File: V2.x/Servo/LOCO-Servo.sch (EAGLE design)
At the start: 49 parts, among them IC1 Atmega 328-P, IC2 MCP2515, IC3 LM340MP-05, Q1 8MHz, Q2 16MHz, X2 2X6-A

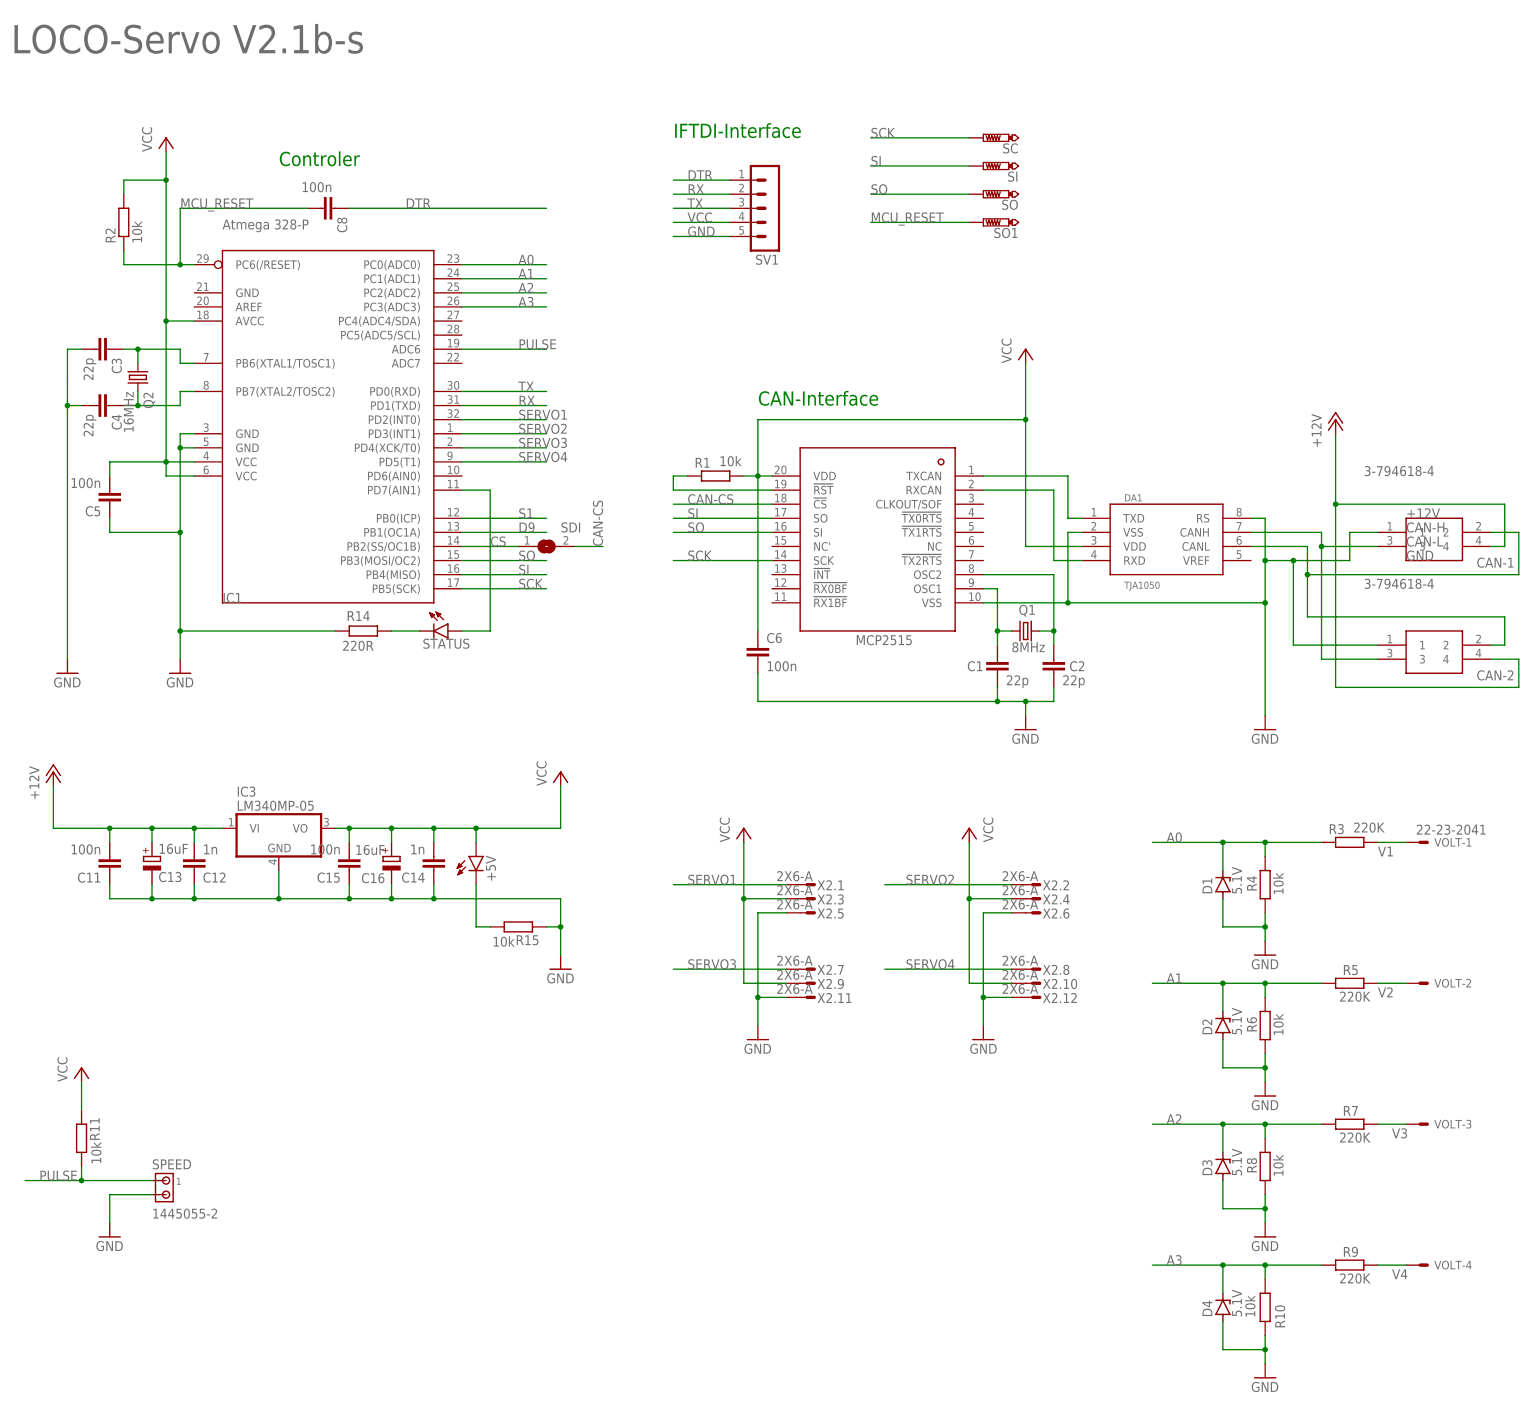
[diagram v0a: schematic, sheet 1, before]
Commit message: added Loco-CAN icon to motor, servo and switch boards
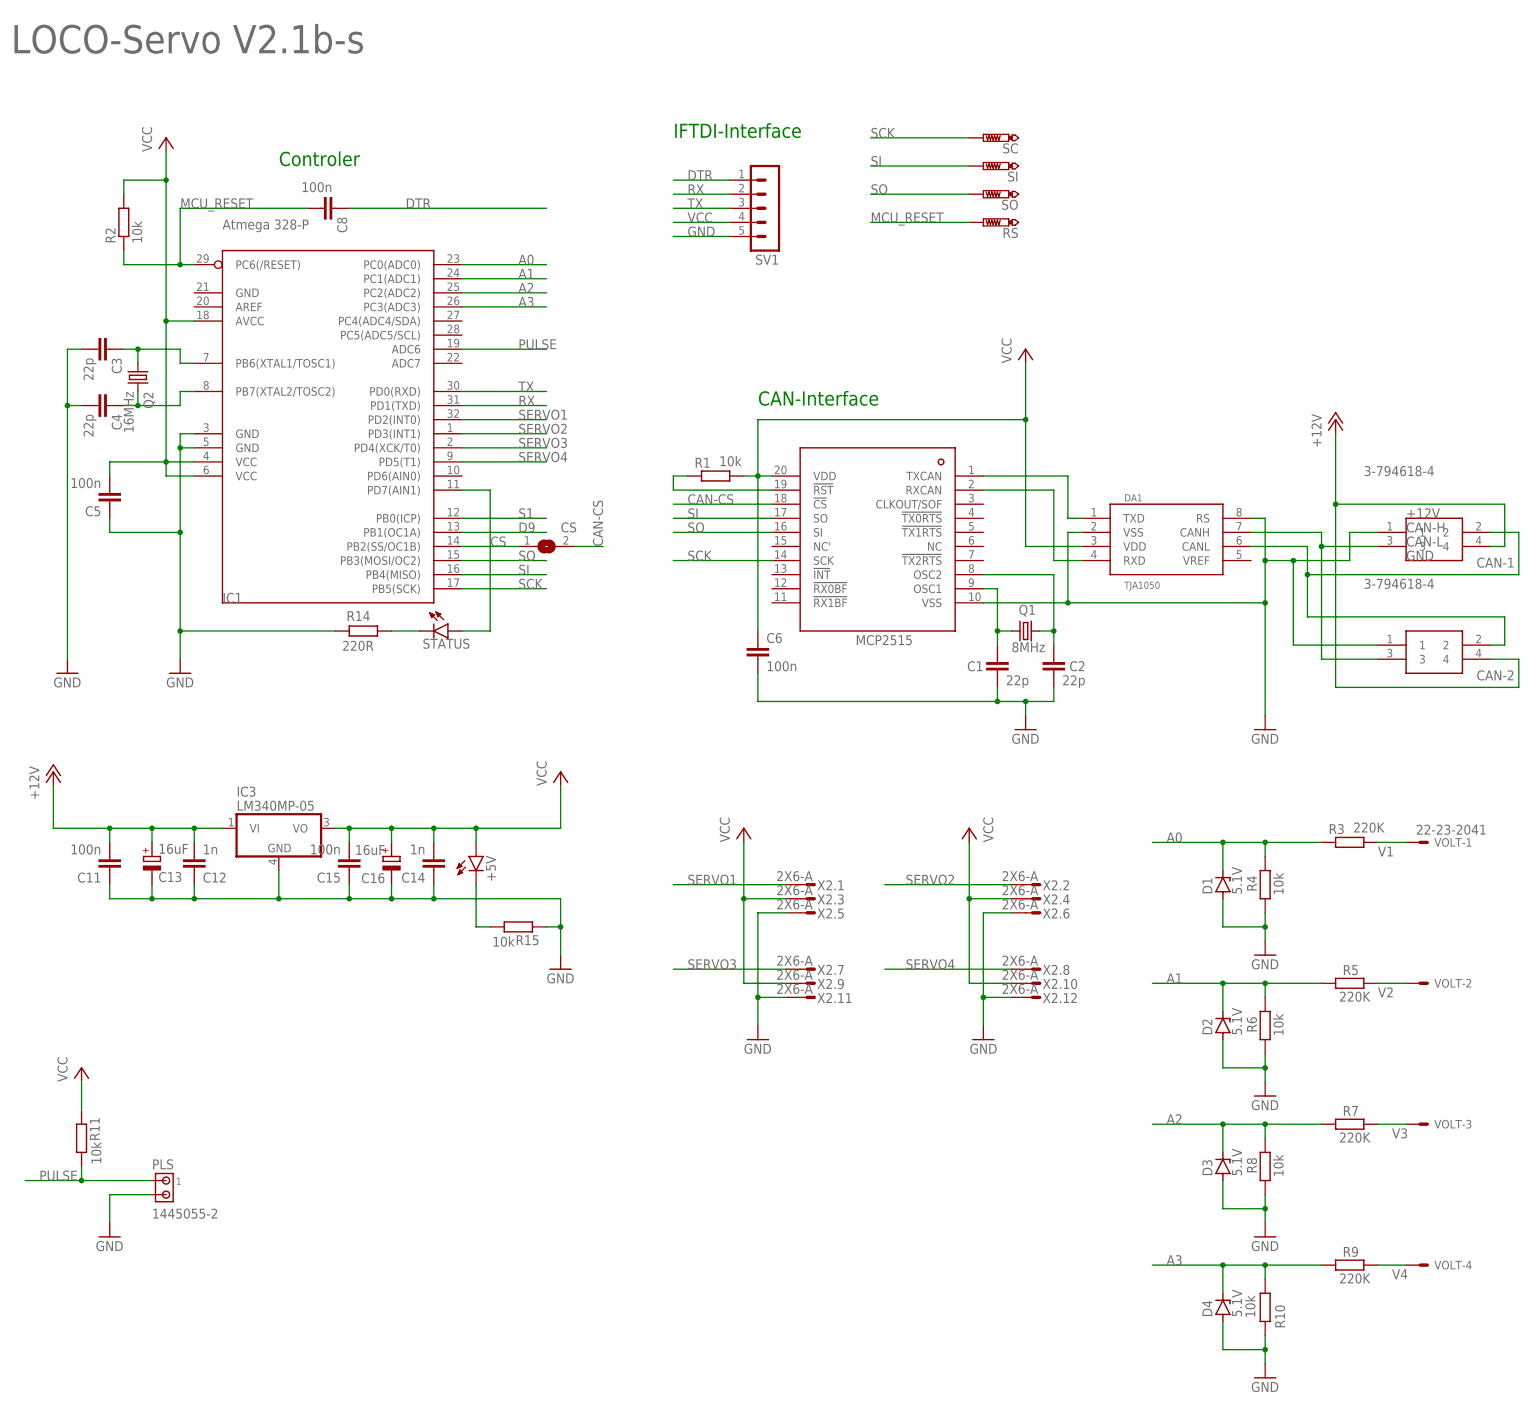
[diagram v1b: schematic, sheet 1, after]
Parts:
- renumbered SDI to CS, SO1 to RS, SPEED to PLS
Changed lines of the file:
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@@
 <part name="D4" library="diode" library_urn="urn:adsk.eagle:library:210" deviceset="ZENER-DIODE" device="SOD80C" package3d_urn="urn:adsk.eagle:package:43405/2" value="5.1V"/>
 <part name="GND12" library="supply1" library_urn="urn:adsk.eagle:library:371" deviceset="GND" device=""/>
-<part name="SPEED" library="con-amp" library_urn="urn:adsk.eagle:library:127" deviceset="1445055-2" device="" package3d_urn="urn:adsk.eagle:package:8081710/1"/>
+<part name="PLS" library="con-amp" library_urn="urn:adsk.eagle:library:127" deviceset="1445055-2" device="" package3d_urn="urn:adsk.eagle:package:8081710/1"/>
 <part name="GND5" library="supply1" library_urn="urn:adsk.eagle:library:371" deviceset="GND" device=""/>
 <part name="R11" library="rcl" library_urn="urn:adsk.eagle:library:334" deviceset="R-EU_" device="MELF0102W" package3d_urn="urn:adsk.eagle:package:23588/2" value="10k"/>
@@
 <part name="SI" library="testpad" library_urn="urn:adsk.eagle:library:385" deviceset="PTR1" device="B1,27" package3d_urn="urn:adsk.eagle:package:27944/2"/>
 <part name="SO" library="testpad" library_urn="urn:adsk.eagle:library:385" deviceset="PTR1" device="B1,27" package3d_urn="urn:adsk.eagle:package:27944/2"/>
-<part name="SDI" library="jumper" library_urn="urn:adsk.eagle:library:252" deviceset="SJ" device="" package3d_urn="urn:adsk.eagle:package:15471/1"/>
+<part name="CS" library="jumper" library_urn="urn:adsk.eagle:library:252" deviceset="SJ" device="" package3d_urn="urn:adsk.eagle:package:15471/1"/>
 <part name="CAN" library="Opto-Electronic" deviceset="LED_CHIP" device="BLUE-1608" package3d_urn="urn:adsk.eagle:package:16655962/3" technology="_" value="STATUS"/>
 <part name="R14" library="rcl" library_urn="urn:adsk.eagle:library:334" deviceset="R-EU_" device="MELF0102W" package3d_urn="urn:adsk.eagle:package:23588/2" value="220R"/>
 <part name="IC3" library="linear" library_urn="urn:adsk.eagle:library:262" deviceset="LM340?-*" device="MP" package3d_urn="urn:adsk.eagle:package:28541/2" technology="05"/>
 <part name="X2" library="con-amp-micro-mate-n-lock" deviceset="2X6" device="-A"/>
-<part name="SO1" library="testpad" library_urn="urn:adsk.eagle:library:385" deviceset="PTR1" device="B1,27" package3d_urn="urn:adsk.eagle:package:27944/2"/>
+<part name="RS" library="testpad" library_urn="urn:adsk.eagle:library:385" deviceset="PTR1" device="B1,27" package3d_urn="urn:adsk.eagle:package:27944/2"/>
 </parts>
 <sheets>
@@
 <attribute name="VALUE" x="198.12" y="-129.54" size="1.778" layer="96"/>
 </instance>
-<instance part="SPEED" gate="G$1" x="2.54" y="-91.44" smashed="yes" rot="MR180" grouprefs="SPEEDO">
+<instance part="PLS" gate="G$1" x="2.54" y="-91.44" smashed="yes" rot="MR180" grouprefs="SPEEDO">
 <attribute name="NAME" x="0" y="-87.63" size="1.778" layer="95" rot="MR180"/>
 <attribute name="VALUE" x="0" y="-96.52" size="1.778" layer="96" rot="MR180"/>
@@
 <attribute name="TP_SIGNAL_NAME" x="152.4" y="87.63" size="1.778" layer="97" rot="R90"/>
 </instance>
-<instance part="SDI" gate="1" x="71.12" y="22.86" smashed="yes" grouprefs="MCU">
+<instance part="CS" gate="1" x="71.12" y="22.86" smashed="yes" grouprefs="MCU">
 <attribute name="NAME" x="73.66" y="25.4" size="1.778" layer="95"/>
 <attribute name="VALUE" x="68.58" y="19.05" size="1.778" layer="96"/>
@@
 <attribute name="VALUE" x="159.766" y="-56.007" size="1.778" layer="96" rot="R180"/>
 </instance>
-<instance part="SO1" gate="G$1" x="149.86" y="81.28" smashed="yes" rot="R90" grouprefs="SPI">
+<instance part="RS" gate="G$1" x="149.86" y="81.28" smashed="yes" rot="R90" grouprefs="SPI">
 <attribute name="NAME" x="156.21" y="80.264" size="1.778" layer="95" rot="R180"/>
 <attribute name="TP_SIGNAL_NAME" x="152.4" y="82.55" size="1.778" layer="97" rot="R90"/>
@@
 </segment>
 <segment>
-<pinref part="SPEED" gate="G$1" pin="2"/>
+<pinref part="PLS" gate="G$1" pin="2"/>
 <pinref part="GND5" gate="1" pin="GND"/>
 <wire x1="0" y1="-93.98" x2="-7.62" y2="-93.98" width="0.1524" layer="91" grouprefs="SPEEDO"/>
@@
 <pinref part="IC1" gate="G$1" pin="PB2(SS/OC1B)"/>
 <label x="60.96" y="22.86" size="1.778" layer="95" grouprefs="MCU"/>
-<pinref part="SDI" gate="1" pin="1"/>
+<pinref part="CS" gate="1" pin="1"/>
 </segment>
 </net>
@@
 </segment>
 <segment>
-<pinref part="SO1" gate="G$1" pin="TP"/>
+<pinref part="RS" gate="G$1" pin="TP"/>
 <wire x1="147.32" y1="81.28" x2="129.54" y2="81.28" width="0.1524" layer="91" grouprefs="SPI"/>
 <label x="129.54" y="81.28" size="1.778" layer="95" grouprefs="SPI"/>
@@
 <net name="CAN-CS" class="0">
 <segment>
-<pinref part="SDI" gate="1" pin="2"/>
+<pinref part="CS" gate="1" pin="2"/>
 <wire x1="76.2" y1="22.86" x2="81.28" y2="22.86" width="0.1524" layer="91" grouprefs="MCU"/>
 <label x="81.28" y="22.86" size="1.778" layer="95" rot="R90" grouprefs="MCU"/>
@@
 <net name="PULSE" class="0">
 <segment>
-<pinref part="SPEED" gate="G$1" pin="1"/>
+<pinref part="PLS" gate="G$1" pin="1"/>
 <wire x1="0" y1="-91.44" x2="-12.7" y2="-91.44" width="0.1524" layer="91" grouprefs="SPEEDO"/>
 <pinref part="R11" gate="G$1" pin="2"/>
